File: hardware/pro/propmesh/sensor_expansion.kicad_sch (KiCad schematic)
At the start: 31 parts

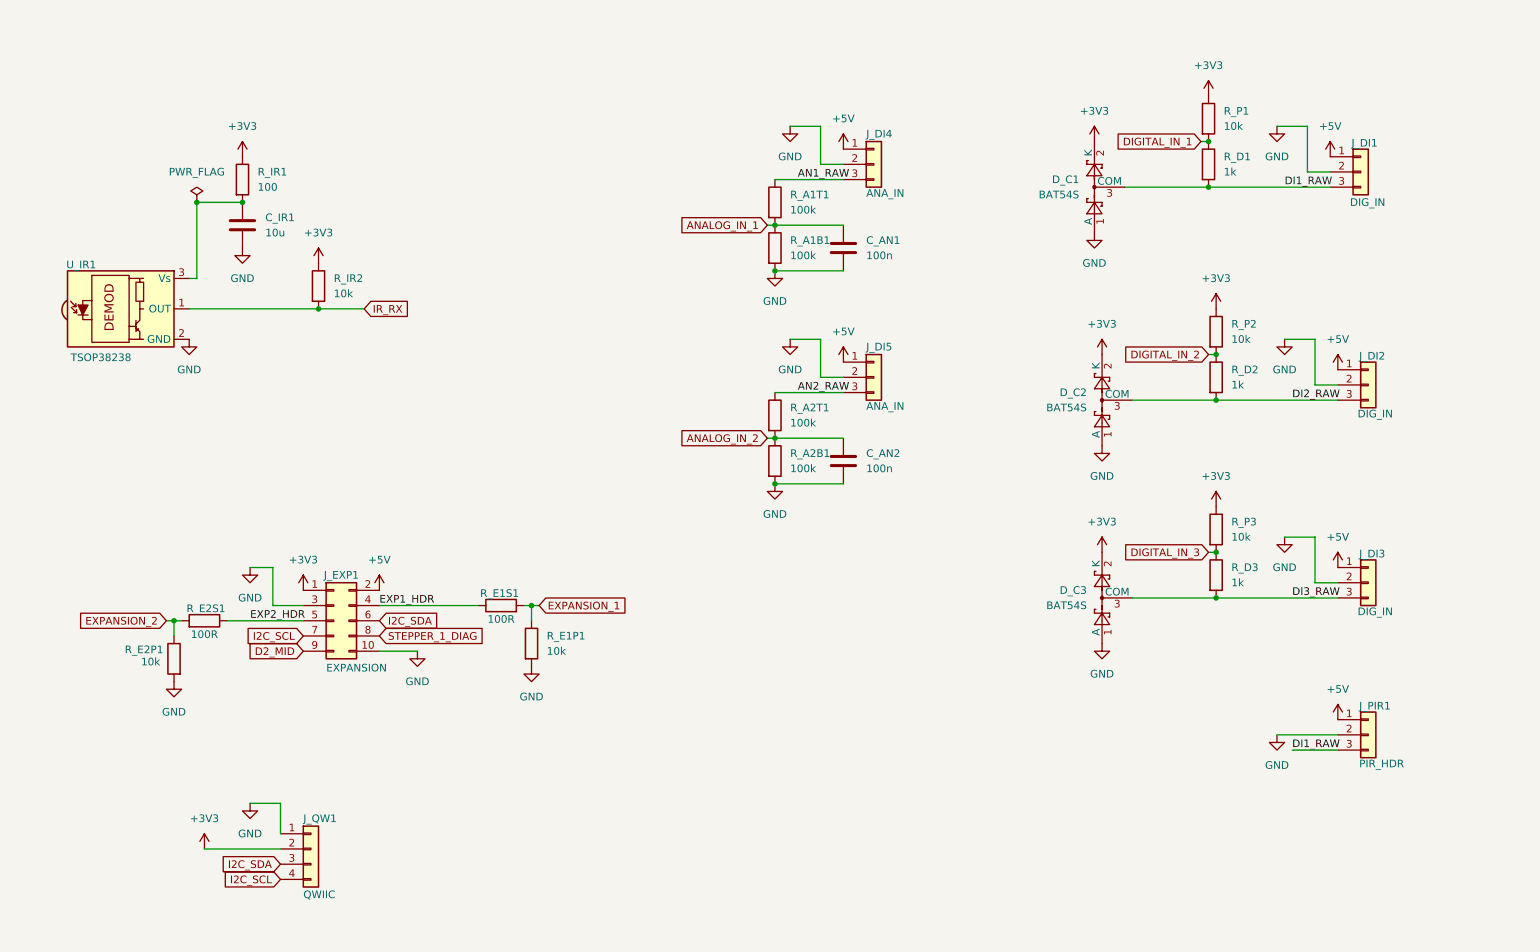
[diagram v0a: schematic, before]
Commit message: Pro schematic complete; enclosure, layout guide, timeline and radio decisions
Schematic: all seven design sheets drawn and green; project-wide ERC at
zero. IR receiver dropped (hidden board can't see a remote — plug-in on
a DIGITAL_IN); GPIO 3 became LED_STRIP_1_CLK; both strip outputs 3- or
4-wire through one octal SN74AHCT541DWR (three revisions of the shifter
in one day, no mode jumpers). Input FET symbol replaced: KiCad 10's
Device:Q_PMOS numbers pins D/G/S and matches no pad — the part would
have been unconnected with no ERC/DRC complaint. All 196 references
renumbered to standard sequential designators (yaml keeps spec names;
the checker prints both). Sheet 08 (test points) and the sheet 01
staged-power link headers specified per spec §2.6 — sheet 01's checker
is red until they are drawn.

checknet.py: symbol pins ⊆ footprint pads check (the silent killer),
multi-unit pin keys + per-unit diagrams (`units:`), symbol-vote sheet
anchoring for half-drawn sheets, orientation-aware net voting, foreign
part reporting, cross-sheet extras no longer crash the report.

Docs: hardware/pro/layout.md — placement by designator, IPC-2221 trace
widths, thermal, silk, ⚠ list, KiCad primer; every chip's datasheet
layout section read (WROOM-1U has NO keep-out; DRV8871 wants a bottom
GND pour; MAX98357A output-trace numbers). Enclosure plan (spec §2.3):
Multilink RNI-1500 / RNI-300, DRiBOX Medium, Joinfworld clear-lid box,
icotek KEL-DPZ entry plate, fit rule 210×140×60 mm inside; PSU
defaults (§2.9) and the 10 A input-path note. Software plan: timeline
design (ramps native, live scrub v1, Cue.start_offset_ms in schema),
yard access (walk-up AP, WireGuard-in-firmware, BYO remote), WiFi-PHY
radio decision vs Zigbee/BLE/LoRa, console served-from-bridge budget,
USB stays in CDC/JTAG mode (no auto-program transistors needed).

Co-Authored-By: Claude Fable 5.1 <noreply@anthropic.com>
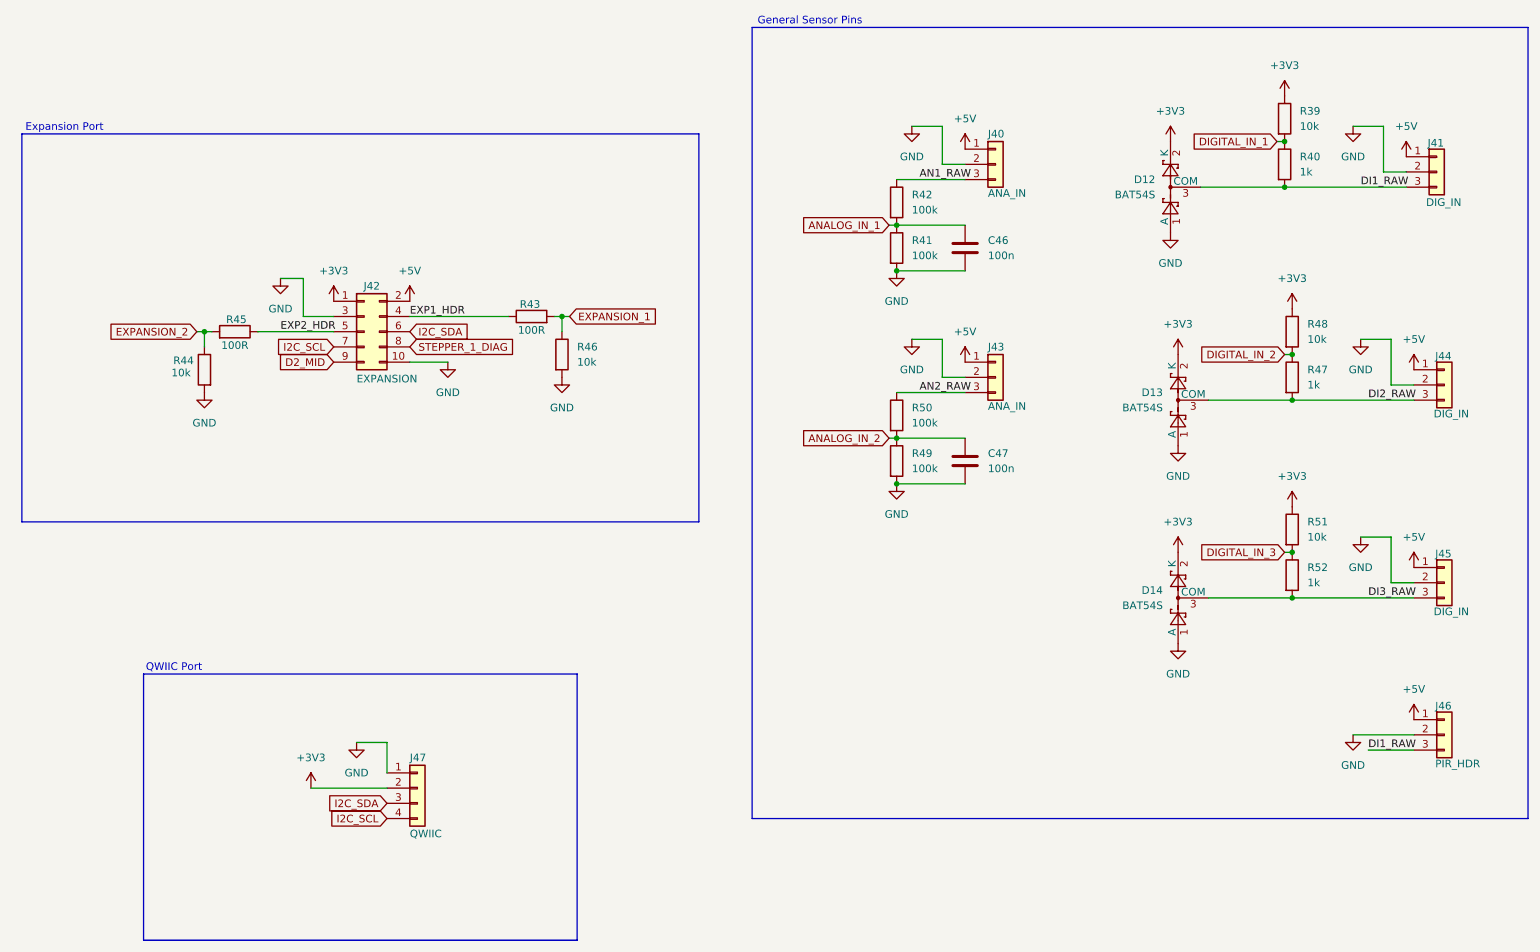
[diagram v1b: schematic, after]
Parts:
- removed C_IR1: 10u, Capacitor_SMD:C_0805_2012Metric, symbol Device:C
- removed R_IR1: 100, Resistor_SMD:R_0603_1608Metric, symbol Device:R
- removed R_IR2: 10k, Resistor_SMD:R_0603_1608Metric, symbol Device:R
- removed U_IR1: TSOP38238, OptoDevice:Vishay_MINICAST-3Pin, symbol Interface_Optical:TSOP382xx
- renumbered C_AN1 to C46, C_AN2 to C47, D_C1 to D12, D_C2 to D13, D_C3 to D14, J_DI4 to J40, J_DI1 to J41, J_EXP1 to J42, J_DI5 to J43, J_DI2 to J44, J_DI3 to J45, J_PIR1 to J46, J_QW1 to J47, R_P1 to R39, R_D1 to R40, R_A1B1 to R41, R_A1T1 to R42, R_E1S1 to R43, R_E2P1 to R44, R_E2S1 to R45, R_E1P1 to R46, R_D2 to R47, R_P2 to R48, R_A2B1 to R49, R_A2T1 to R50, R_P3 to R51, R_D3 to R52
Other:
- note added: "Expansion Port"
- note added: "General Sensor Pins"
- note added: "QWIIC Port"
- moved on the sheet: C46, C47, D12, D13, D14, J40, J41, J42, J43, J44, J45, J46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

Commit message: Pro v0.1: board setup + placement, two design reviews applied, datasheet-review changes specced
Checkpoint of two weeks' work since dacce25. The schematic is MID-EDIT:
sheets 02/04/05/07/08 checkers are red by design until the changes in
hardware/pro/schematic-changes-2026-09-16.md are drawn; sheet 03 is
half-drawn (see finish-v0.1.md).

Layout
- layout.md rebuilt as one ordered procedure (Part A) with a
  where-you-are line; Board Setup, outline, origin, frozen 120x90 hole
  pattern; routing and pour guidance; per-net noise keep-outs
- tools: checksetup.py (setup/outline/holes/netclasses/socket rows),
  placeboard.py, placetps.py (test points on B.Cu for bodge + pogo rig),
  setpos.py, snapgrid.py; placement renders; power/MCU placement tables

Reviews
- review-2026-09-08 (external audit): C1 EN cap, MA/MB_ILIM short,
  servo/output channel order, sensor clamp order, VIN_FUSED label,
  F1 footprint — all fixed in the schematic
- checknet.py: merged-net assertion (distinct spec nets must be
  distinct schematic nets) — the class that hid the ILIM short
- review-2026-09-16 (routing) + datasheet-review-2026-09-16 with a
  verified disposition; Mini plan audit + recommendations (other session)

Decisions 2026-09-16 (specs, pinmap and headers updated; drawing pending)
- 5 V rail: strip bulk 1000 uF -> 220 uF Rubycon C88757; JP_USB link
  makes USB power opt-in (AP64350 hiccups into 2 mF)
- sensor series R 1 k 0603 -> 2.2 k 1206 C17948 (24 V miswire)
- second PCA9685 (0x41, 1 kHz) for the six DC channels; servos stay at
  50 Hz on 0x40; both OE on GPIO 37 = PCA_OE with pull-up (pinmap:
  36/36 GPIO used; genpins.py supports several PCA9685s)
- output FETs Q1-Q6 -> 40 V Vishay SI2356DS C74127 (TVS coordination)
- SD DAT1/DAT2 pull-ups; USB 22R pair + DNP caps + VBUS 100 nF;
  74AHCT541 input pulldowns, R53 fitted
- MP6603 dual-mode socket mapping verified; MS strap defaults decided

Co-Authored-By: Claude Opus 5 (1M context) <noreply@anthropic.com>
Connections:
- net DI1_RAW: no longer D12.3 (COM)
- net DI2_RAW: no longer D13.3 (COM)
- net DI3_RAW: no longer D14.3 (COM)
- net DIGITAL_IN_1: now also D12.3 (COM)
- net DIGITAL_IN_2: now also D13.3 (COM)
- net DIGITAL_IN_3: now also D14.3 (COM)
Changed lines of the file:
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@@
-	)
-	(junction
-		(at 238.76 81.28)
-		(diameter 0)
-		(color 0 0 0 0)
 	)
 	(junction
@@
 	)
 	(junction
-		(at 238.76 114.3)
-		(diameter 0)
-		(color 0 0 0 0)
-	)
-	(junction
 		(at 238.76 106.68)
 		(diameter 0)
@@
 		(color 0 0 0 0)
 	)
-	(junction
-		(at 237.49 45.72)
-		(diameter 0)
-		(color 0 0 0 0)
-	)
 	(wire
 		(pts
@@
 	(wire
 		(pts
+			(xy 228.6 73.66) (xy 228.6 81.28)
+		)
+		(stroke
+			(width 0)
+			(type default)
+		)
+	)
+	(wire
+		(pts
 			(xy 184.15 87.63) (xy 172.72 87.63)
 		)
@@
 	(wire
 		(pts
+			(xy 228.6 106.68) (xy 238.76 106.68)
+		)
+		(stroke
+			(width 0)
+			(type default)
+		)
+	)
+	(wire
+		(pts
 			(xy 172.72 95.25) (xy 184.15 95.25)
 		)
@@
 	(wire
 		(pts
+			(xy 228.6 38.1) (xy 228.6 45.72)
+		)
+		(stroke
+			(width 0)
+			(type default)
+		)
+	)
+	(wire
+		(pts
 			(xy 180.34 71.12) (xy 180.34 77.47)
 		)
@@
 	(wire
 		(pts
-			(xy 237.49 73.66) (xy 238.76 73.66)
+			(xy 228.6 81.28) (xy 224.79 81.28)
 		)
 		(stroke
@@
 	(wire
 		(pts
-			(xy 236.22 38.1) (xy 237.49 38.1)
-		)
-		(stroke
-			(width 0)
-			(type default)
-		)
-	)
-	(wire
-		(pts
 			(xy 238.76 114.3) (xy 259.08 114.3)
 		)
@@
 	(wire
 		(pts
-			(xy 224.79 114.3) (xy 238.76 114.3)
-		)
-		(stroke
-			(width 0)
-			(type default)
-		)
-	)
-	(wire
-		(pts
 			(xy 69.85 60.96) (xy 73.66 60.96)
 		)
@@
 	(wire
 		(pts
+			(xy 228.6 45.72) (xy 223.52 45.72)
+		)
+		(stroke
+			(width 0)
+			(type default)
+		)
+	)
+	(wire
+		(pts
 			(xy 175.26 71.12) (xy 180.34 71.12)
 		)
@@
 	(wire
 		(pts
+			(xy 228.6 73.66) (xy 238.76 73.66)
+		)
+		(stroke
+			(width 0)
+			(type default)
+		)
+	)
+	(wire
+		(pts
 			(xy 57.15 72.39) (xy 57.15 69.85)
 		)
@@
 	(wire
 		(pts
-			(xy 237.49 106.68) (xy 238.76 106.68)
+			(xy 228.6 106.68) (xy 228.6 114.3)
 		)
 		(stroke
@@
 	(wire
 		(pts
-			(xy 223.52 45.72) (xy 237.49 45.72)
-		)
-		(stroke
-			(width 0)
-			(type default)
-		)
-	)
-	(wire
-		(pts
 			(xy 180.34 35.56) (xy 180.34 41.91)
 		)
@@
 	(wire
 		(pts
+			(xy 228.6 114.3) (xy 224.79 114.3)
+		)
+		(stroke
+			(width 0)
+			(type default)
+		)
+	)
+	(wire
+		(pts
+			(xy 228.6 38.1) (xy 237.49 38.1)
+		)
+		(stroke
+			(width 0)
+			(type default)
+		)
+	)
+	(wire
+		(pts
 			(xy 184.15 52.07) (xy 172.72 52.07)
 		)
@@
 		(pts
 			(xy 73.66 60.96) (xy 73.66 67.31)
-		)
-		(stroke
-			(width 0)
-			(type default)
-		)
-	)
-	(wire
-		(pts
-			(xy 224.79 81.28) (xy 238.76 81.28)
 		)
 		(stroke
@@
 	(global_label "DIGITAL_IN_3"
 		(shape input)
-		(at 237.49 106.68 180)
+		(at 228.6 106.68 90)
 		(fields_autoplaced yes)
 		(effects
@@
 				(size 1.27 1.27)
 			)
-			(justify right)
+			(justify left)
 		)
 		(property "Intersheetrefs" "${INTERSHEET_REFS}"
-			(at 222.5909 106.68 0)
+			(at 228.6 91.7809 90)
 			(hide yes)
 			(show_name no)
@@
 					(size 1.27 1.27)
 				)
-				(justify right)
+				(justify left)
 			)
 		)
@@
 	(global_label "DIGITAL_IN_1"
 		(shape input)
-		(at 236.22 38.1 180)
+		(at 228.6 38.1 90)
 		(fields_autoplaced yes)
 		(effects
@@
 				(size 1.27 1.27)
 			)
-			(justify right)
+			(justify left)
 		)
 		(property "Intersheetrefs" "${INTERSHEET_REFS}"
-			(at 221.3209 38.1 0)
+			(at 228.6 23.2009 90)
 			(hide yes)
 			(show_name no)
@@
 					(size 1.27 1.27)
 				)
-				(justify right)
+				(justify left)
 			)
 		)
@@
 	(global_label "DIGITAL_IN_2"
 		(shape input)
-		(at 237.49 73.66 180)
+		(at 228.6 73.66 90)
 		(fields_autoplaced yes)
 		(effects
@@
 				(size 1.27 1.27)
 			)
-			(justify right)
+			(justify left)
 		)
 		(property "Intersheetrefs" "${INTERSHEET_REFS}"
-			(at 222.5909 73.66 0)
+			(at 228.6 58.7609 90)
 			(hide yes)
 			(show_name no)
@@
 					(size 1.27 1.27)
 				)
-				(justify right)
-			)
-		)
+				(justify left)
+			)
+		)

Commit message: Pro v0.1 schematic complete; board cleanup pass, parity 0
Schematic: all datasheet-review changes drawn (decisions 1A, 2A, 3B,
OE on GPIO 37, 4B). All eight sheet checkers ALL NETS MATCH, ERC 0
errors / 0 warnings, pinmap matches generated headers.
- sheet 03: second PCA9685 (U12, 0x41) with B-straps, PCA_OE net with
  10k pull-up (R59); DC FETs Q1-Q6 = SI2356DS
- sheets 02/04/05/07/08: USB link/22R/VBUS cap, SD DAT1/DAT2 pull-ups,
  shifter pulldowns, 2.2k 1206 sensor Rs; R53 (GPIO3 pulldown) now drawn
  on sheet 05, specs moved to match

Board (KiCad closed, backup kept):
- F8 done, schematic parity 0; orphan DNP R53 removed
- mounting holes H1-H4, board-only, excluded from BOM/position files
- minimum drill 0.3 -> 0.2 mm: U2's own 0.2/0.6 thermal vias; JLCPCB
  4-layer standard cost for 0.2 mm holes with >= 0.45 mm pads
- DG128-02P pads 2.3 -> 2.8 mm (J17 10 A input; library edited too)
- DRV8871 exposed-pad paste inset 0.1 mm (library edited too)
- 43 parts snapped to grid; snapgrid.py now exempts J20/J22 so the
  StepStick rows stay 12.70 mm
- DRC: 11 courtyard overlaps left (3 accepted terminal gangs, 8 in the
  sensor corner from the 1206 resistors) + silkscreen

Tools: checknet.py net vote ignores orientation for R/C/L (three
upside-down pull-ups had out-voted the chip pin on sheet 04); verified
it still catches a shorted net and a mis-wired pull-up.
checksetup.py: min drill 0.2.

Also includes the Mini module selection and KiCad project started in
another session (2026-09-19).

Co-Authored-By: Claude Opus 5.5 <noreply@anthropic.com>
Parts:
- R40, R47, R52: value 1k -> 2.2k; footprint Resistor_SMD:R_0603_1608Metric -> Resistor_SMD:R_1206_3216Metric
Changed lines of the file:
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@@
 			)
 		)
-		(property "Value" "1k"
+		(property "Value" "2.2k"
 			(at 240.03 43.1799 0)
 			(show_name no)
@@
 			)
 		)
-		(property "Footprint" "Resistor_SMD:R_0603_1608Metric"
+		(property "Footprint" "Resistor_SMD:R_1206_3216Metric"
 			(at 235.712 41.91 90)
 			(hide yes)
@@
 			)
 		)
-		(property "Value" "1k"
+		(property "Value" "2.2k"
 			(at 241.3 78.7399 0)
 			(show_name no)
@@
 			)
 		)
-		(property "Footprint" "Resistor_SMD:R_0603_1608Metric"
+		(property "Footprint" "Resistor_SMD:R_1206_3216Metric"
 			(at 236.982 77.47 90)
 			(hide yes)
@@
 			)
 		)
-		(property "Value" "1k"
+		(property "Value" "2.2k"
 			(at 241.3 111.7599 0)
 			(show_name no)
@@
 			)
 		)
-		(property "Footprint" "Resistor_SMD:R_0603_1608Metric"
+		(property "Footprint" "Resistor_SMD:R_1206_3216Metric"
 			(at 236.982 110.49 90)
 			(hide yes)
